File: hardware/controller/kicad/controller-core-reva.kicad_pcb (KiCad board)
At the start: 2 copper layers, 141.6 x 135.2 mm, 135 parts, among them J101 12V_ISOLATED_INPUT / JST XH, J102 STM_SWD / 1x6 2.54mm, J103 ESP_UART / 1x6 2.54mm, J104 UI_LINK / IDC 2x8 2.54mm, J105 JP13 NTC / 2 vías, J106 JP5 FLOW ADAPTER / VCC-GND-OC, J107 JP14 DOOR / contacto seco, J108 JP16 VISUAL V1..V8 / XH-8, J109 JP22 WATER / RED-WHITE-BLACK, J110 USB-C SERVICE / USB 2.0, J111 USB BENCH POWER / OPEN, J112 24V_ACTUATOR_INPUT / JST XH, J113 JP3 VALVE / JST XH, J114 POWER MONITOR / MEASURE ONLY, Q501 SI2308A, U101 STM32G431RBT6, U201 ESP32-S3-WROOM-1-N8R8, U203 USBLC6-2SC6, U301 AP63203WU-7, U302 TPS22918DBVR, U501 DRV8876PWPR, U502 UCC27517DBVR, U601 TPS3828-33DBVR, U602 SN74LVC2G08DCTR

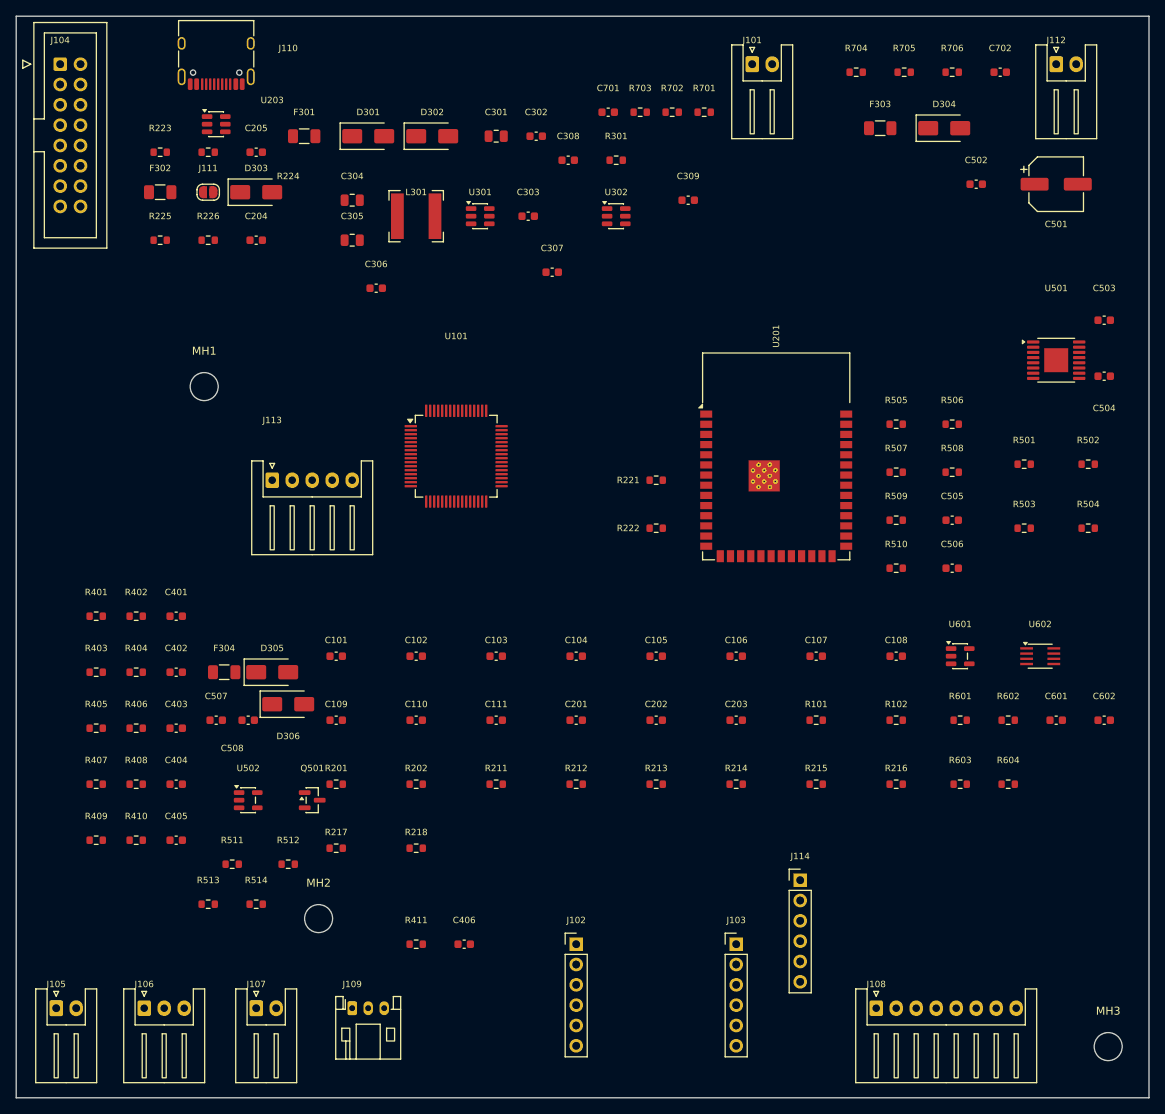
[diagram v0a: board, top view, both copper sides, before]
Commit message: Place controller PCB by functional blocks
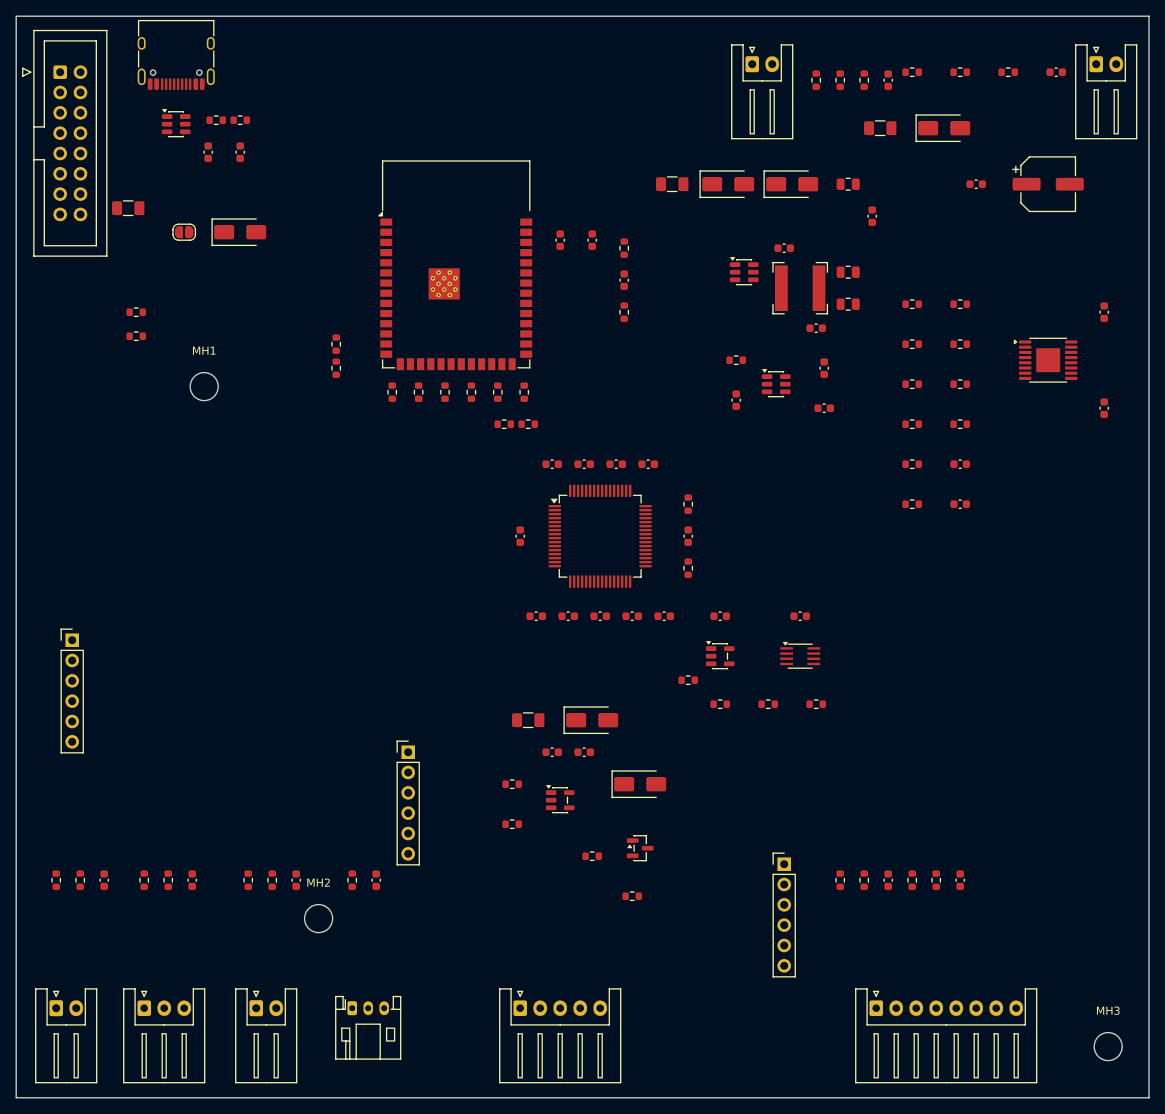
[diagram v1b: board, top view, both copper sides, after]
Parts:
- moved R409 102.1 mm to (112.0, 108.0), turned to 90 degrees
- moved R410 100.1 mm to (115.0, 108.0), turned to 90 degrees
- moved C405 98.1 mm to (118.0, 108.0), turned to 90 degrees
- moved R407 93.8 mm to (103.0, 108.0), turned to 90 degrees
- moved R408 91.8 mm to (106.0, 108.0), turned to 90 degrees
- moved J103 91.3 mm to (7.00, 78.0)
- moved C404 89.8 mm to (109.0, 108.0), turned to 90 degrees
- moved R201 76.1 mm to (76.0, 29.0), turned to 90 degrees
- moved J113 72.9 mm to (63.0, 124.0)
- moved R216 72.3 mm to (56.9, 47.0), turned to 90 degrees
- moved R215 67.5 mm to (53.6, 47.0), turned to 90 degrees
- moved R202 64.5 mm to (76.0, 37.0), turned to 90 degrees
- moved R214 63.1 mm to (50.3, 47.0), turned to 90 degrees
- moved C304 62.6 mm to (104.0, 32.0)
- moved C203 62.6 mm to (72.0, 28.0), turned to 90 degrees
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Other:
- board text added: "FUNCTIONAL PLACEMENT / NOT FOR FABRICATION Rev A low-voltage blocks placed; copper routing pending"
- board text removed: "UNROUTED COMPONENT STAGING / NOT FOR FABRICATION Rev A mechanics accepted; low-voltage connectors and power staged; routing pending"

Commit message: Align controller connectors with original PCB
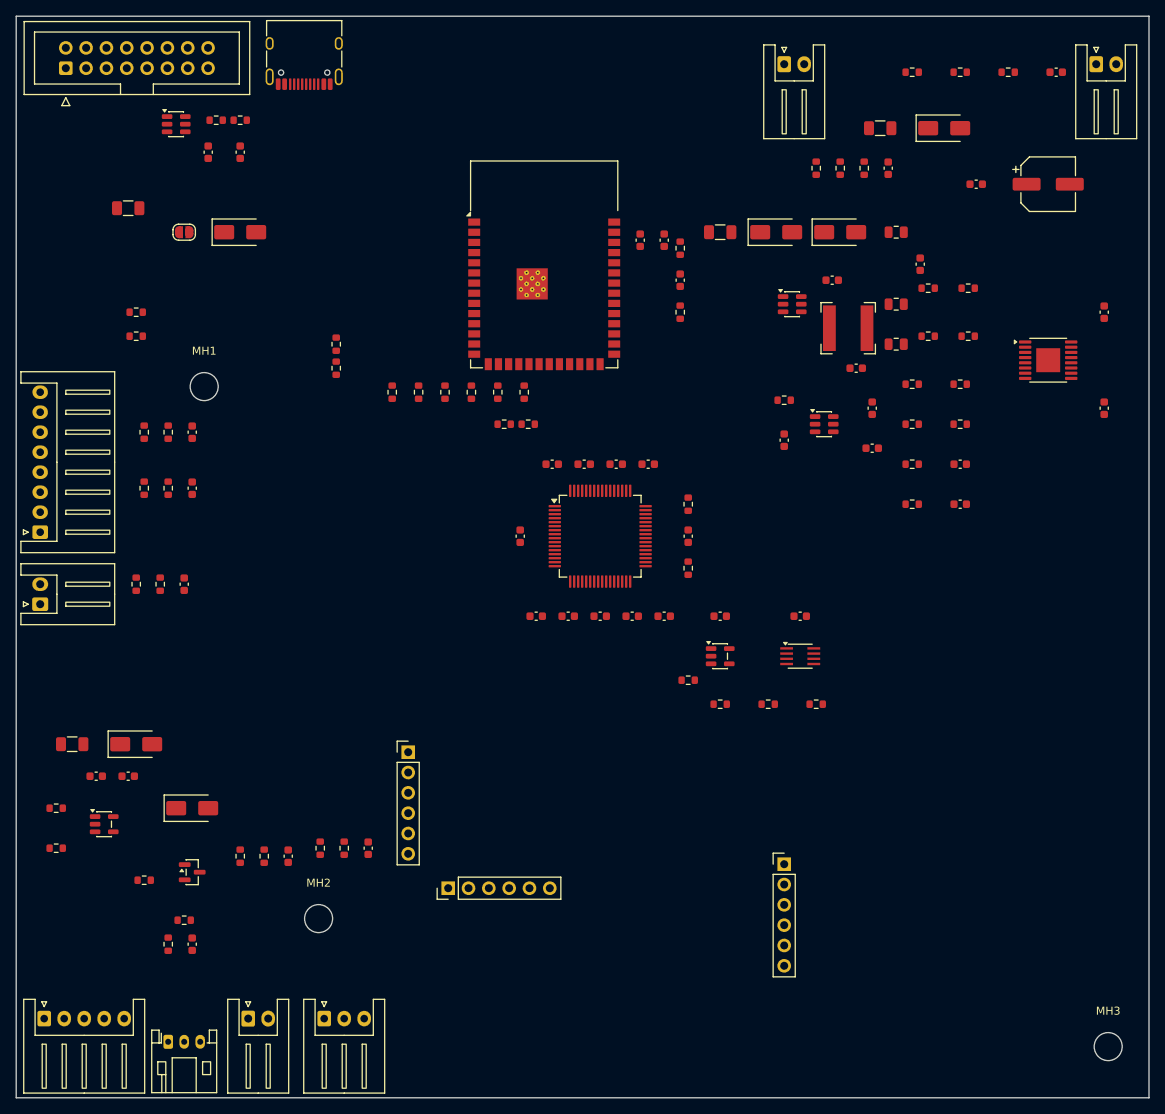
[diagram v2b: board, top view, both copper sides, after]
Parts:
- moved J108 120.3 mm to (3.00, 64.5), turned to 90 degrees
- moved C405 107.8 mm to (22.0, 59.0)
- moved R409 107.8 mm to (16.0, 59.0)
- moved R410 107.8 mm to (19.0, 59.0)
- moved C404 103.5 mm to (22.0, 52.0)
- moved R407 103.5 mm to (16.0, 52.0)
- moved R408 103.5 mm to (19.0, 52.0)
- moved J113 59.5 mm to (3.50, 125.3)
- moved J107 57.3 mm to (3.00, 73.5), turned to 90 degrees
- moved C507 57.1 mm to (10.0, 95.0)
- moved C508 57.1 mm to (14.0, 95.0)
- moved D305 57.1 mm to (15.0, 91.0)
- moved F304 57.1 mm to (7.00, 91.0)
- moved R511 57.1 mm to (5.00, 99.0)
- moved R512 57.1 mm to (5.00, 104.0)
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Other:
- board text added: "MECHANICAL CONNECTOR PLACEMENT / NOT FOR FABRICATION Original harness positions estimated from IMG_1098/1101; copper pending"
- board text removed: "FUNCTIONAL PLACEMENT / NOT FOR FABRICATION Rev A low-voltage blocks placed; copper routing pending"

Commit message: Define controller fabrication and routing rules
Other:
- copper layers 2 -> 4
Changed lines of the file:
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@@
 	(layers
 		(0 "F.Cu" signal)
+		(4 "In1.Cu" signal)
+		(6 "In2.Cu" signal)
 		(2 "B.Cu" signal)
 		(9 "F.Adhes" user "F.Adhesive")
@@
 		)
 		(zone
-			(layers "F.Cu" "B.Cu")
+			(layers "F.Cu" "B.Cu" "In1.Cu" "In2.Cu")
 			(hatch full 0.508)
 			(connect_pads
@@
 	)
 	(zone
-		(layers "F.Cu" "B.Cu")
-		(name "reserved original connector JP9")
+		(layers "F.Cu" "B.Cu" "In1.Cu" "In2.Cu")
+		(name "reserved original connector JP24")
 		(hatch edge 0.5)
 		(connect_pads
@@
 		(polygon
 			(pts
-				(xy 125.5 118) (xy 130.5 118) (xy 130.5 130) (xy 125.5 130)
+				(xy 89 121) (xy 97 121) (xy 97 135) (xy 89 135)
 			)
 		)
 	)
 	(zone
-		(layers "F.Cu" "B.Cu")
-		(name "reserved original connector JP19")
+		(layers "F.Cu" "B.Cu" "In1.Cu" "In2.Cu")
+		(name "reserved original connector JP8")
 		(hatch edge 0.5)
 		(connect_pads
@@
 		(polygon
 			(pts
-				(xy 73 119) (xy 88 119) (xy 88 135) (xy 73 135)
+				(xy 57 121) (xy 69 121) (xy 69 135) (xy 57 135)
 			)
 		)
 	)
 	(zone
-		(layers "F.Cu" "B.Cu")
-		(name "reserved original connector JP24")
+		(layers "F.Cu" "B.Cu" "In1.Cu" "In2.Cu")
+		(name "reserved original connector JP17")
 		(hatch edge 0.5)
 		(connect_pads
@@
 		(polygon
 			(pts
-				(xy 89 121) (xy 97 121) (xy 97 135) (xy 89 135)
+				(xy 104 119) (xy 116 119) (xy 116 135) (xy 104 135)
 			)
 		)
 	)
 	(zone
-		(layers "F.Cu" "B.Cu")
+		(layers "F.Cu" "B.Cu" "In1.Cu" "In2.Cu")
 		(name "reserved original connector JP1")
 		(hatch edge 0.5)
@@
 	)
 	(zone
-		(layers "F.Cu" "B.Cu")
-		(name "reserved original connector JP17")
+		(layers "F.Cu" "B.Cu" "In1.Cu" "In2.Cu")
+		(name "reserved original connector JP9")
 		(hatch edge 0.5)
 		(connect_pads
@@
 		(polygon
 			(pts
-				(xy 104 119) (xy 116 119) (xy 116 135) (xy 104 135)
+				(xy 125.5 118) (xy 130.5 118) (xy 130.5 130) (xy 125.5 130)
 			)
 		)
 	)
 	(zone
-		(layers "F.Cu" "B.Cu")
-		(name "reserved original connector JP8")
+		(layers "F.Cu" "B.Cu" "In1.Cu" "In2.Cu")
+		(name "reserved original connector JP19")
 		(hatch edge 0.5)
 		(connect_pads
@@
 		(polygon
 			(pts
-				(xy 57 121) (xy 69 121) (xy 69 135) (xy 57 135)
+				(xy 73 119) (xy 88 119) (xy 88 135) (xy 73 135)
 			)
 		)

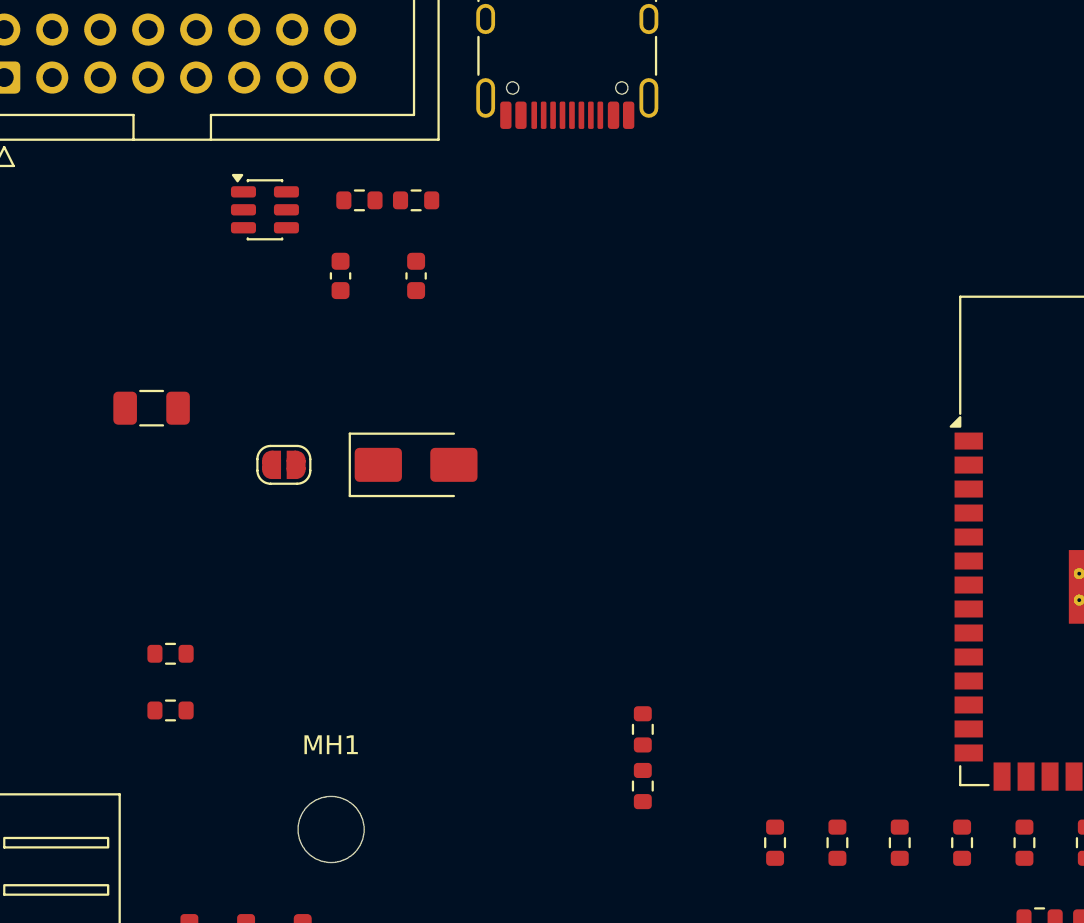
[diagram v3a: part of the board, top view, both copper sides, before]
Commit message: Integrate full-board mains scope and route USB
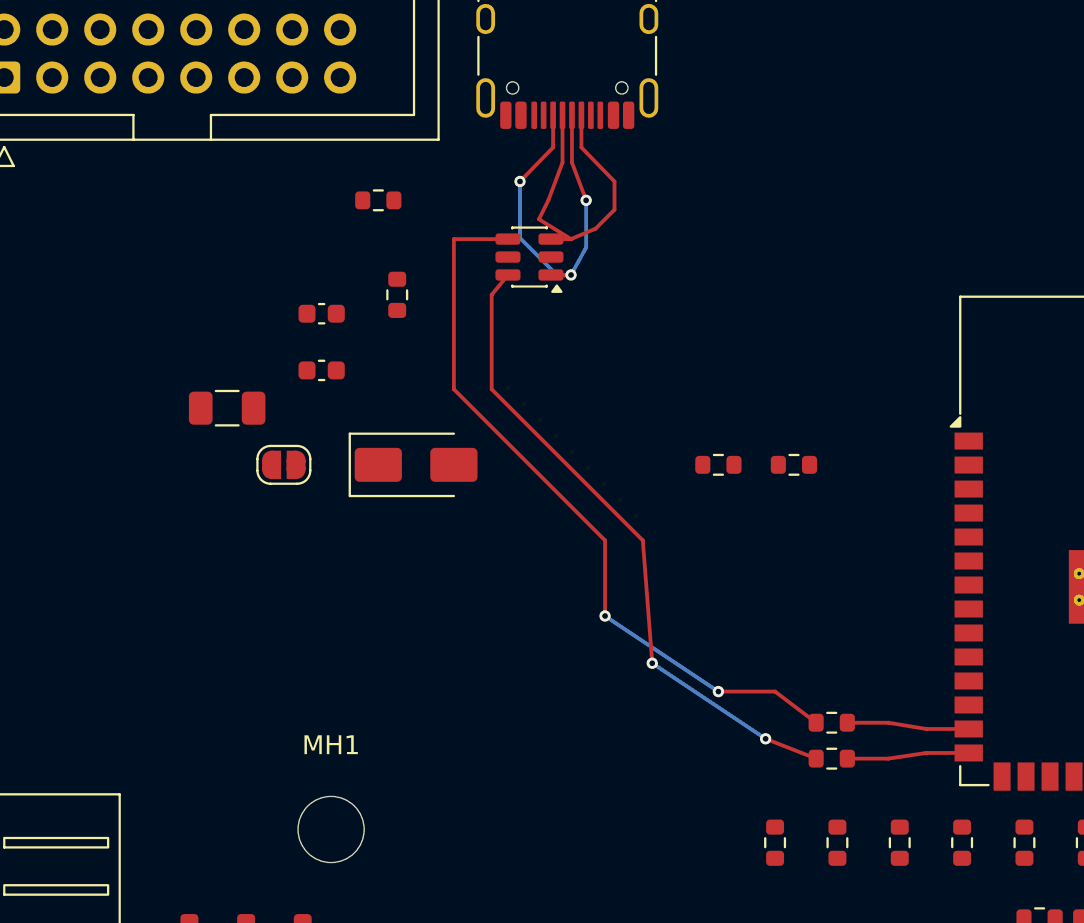
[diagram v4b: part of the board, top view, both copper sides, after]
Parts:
- moved R224 35.5 mm to (48.0, 27.0)
- moved R223 30.7 mm to (44.0, 27.0)
- moved U203 14.2 mm to (34.0, 16.0), turned to 180 degrees
- moved R222 10.1 mm to (50.0, 42.5), turned to 0 degrees
- moved R221 10.0 mm to (50.0, 40.6), turned to 0 degrees
- moved C204 5.39 mm to (23.0, 19.0), turned to 0 degrees
- moved C205 5.10 mm to (23.0, 22.0), turned to 0 degrees
- moved R226 5.10 mm to (27.0, 18.0), turned to 90 degrees
- moved F302 4.00 mm to (18.0, 24.0)
- moved R225 1.00 mm to (26.0, 13.0)
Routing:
- net /USB_DM_DEVICE: track 0.00 -> 39.1 mm, vias 0 -> 2
- net /USB_DP_DEVICE: track 0.00 -> 34.3 mm, vias 0 -> 2
- net /USB_DP_PORT: track 0.00 -> 20.6 mm, vias 0 -> 3
- net /USB_DM_PORT: track 0.00 -> 17.4 mm
- net /USB_DM_RAW: track 0.00 -> 6.45 mm
- net /USB_DP_RAW: track 0.00 -> 6.45 mm
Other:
- copper layers 4 -> 2

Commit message: Add original mains and load connectors
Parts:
- added J115: JP8 GRINDER / 320VDC, Connector_JST:JST_VH_S3P-VH_1x03_P3.96mm_Horizontal, F.Cu at (59.0, 120.8)
- added J117: JP24 PUMP / 230VAC, Connector_JST:JST_VH_S2P-VH_1x02_P3.96mm_Horizontal, F.Cu at (91.0, 120.8)
- added J118: JP17 MAINS / L-N, Connector_JST:JST_VH_S3P-VH_1x03_P3.96mm_Horizontal, F.Cu at (106.0, 121.3)
- moved J114 11.2 mm to (106.0, 101.0)
